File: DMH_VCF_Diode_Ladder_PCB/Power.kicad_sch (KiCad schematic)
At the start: 14 parts, among them J0 Conn_01x01, J100 IDC_02x08, J101 IDC_02x05

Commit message: Main schematic in progress
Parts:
- added C8, C9: 100nF, Capacitor_THT:C_Disc_D4.3mm_W1.9mm_P5.00mm, symbol Device:C
- added U1: TL074, Package_DIP:DIP-14_W7.62mm_Socket, symbol Amplifier_Operational:TL074
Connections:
- net +12V: now also C8.1, U1.4 (V+)
- net -12V: now also C9.2, U1.11 (V-)
- net GND: now also C8.2, C9.1

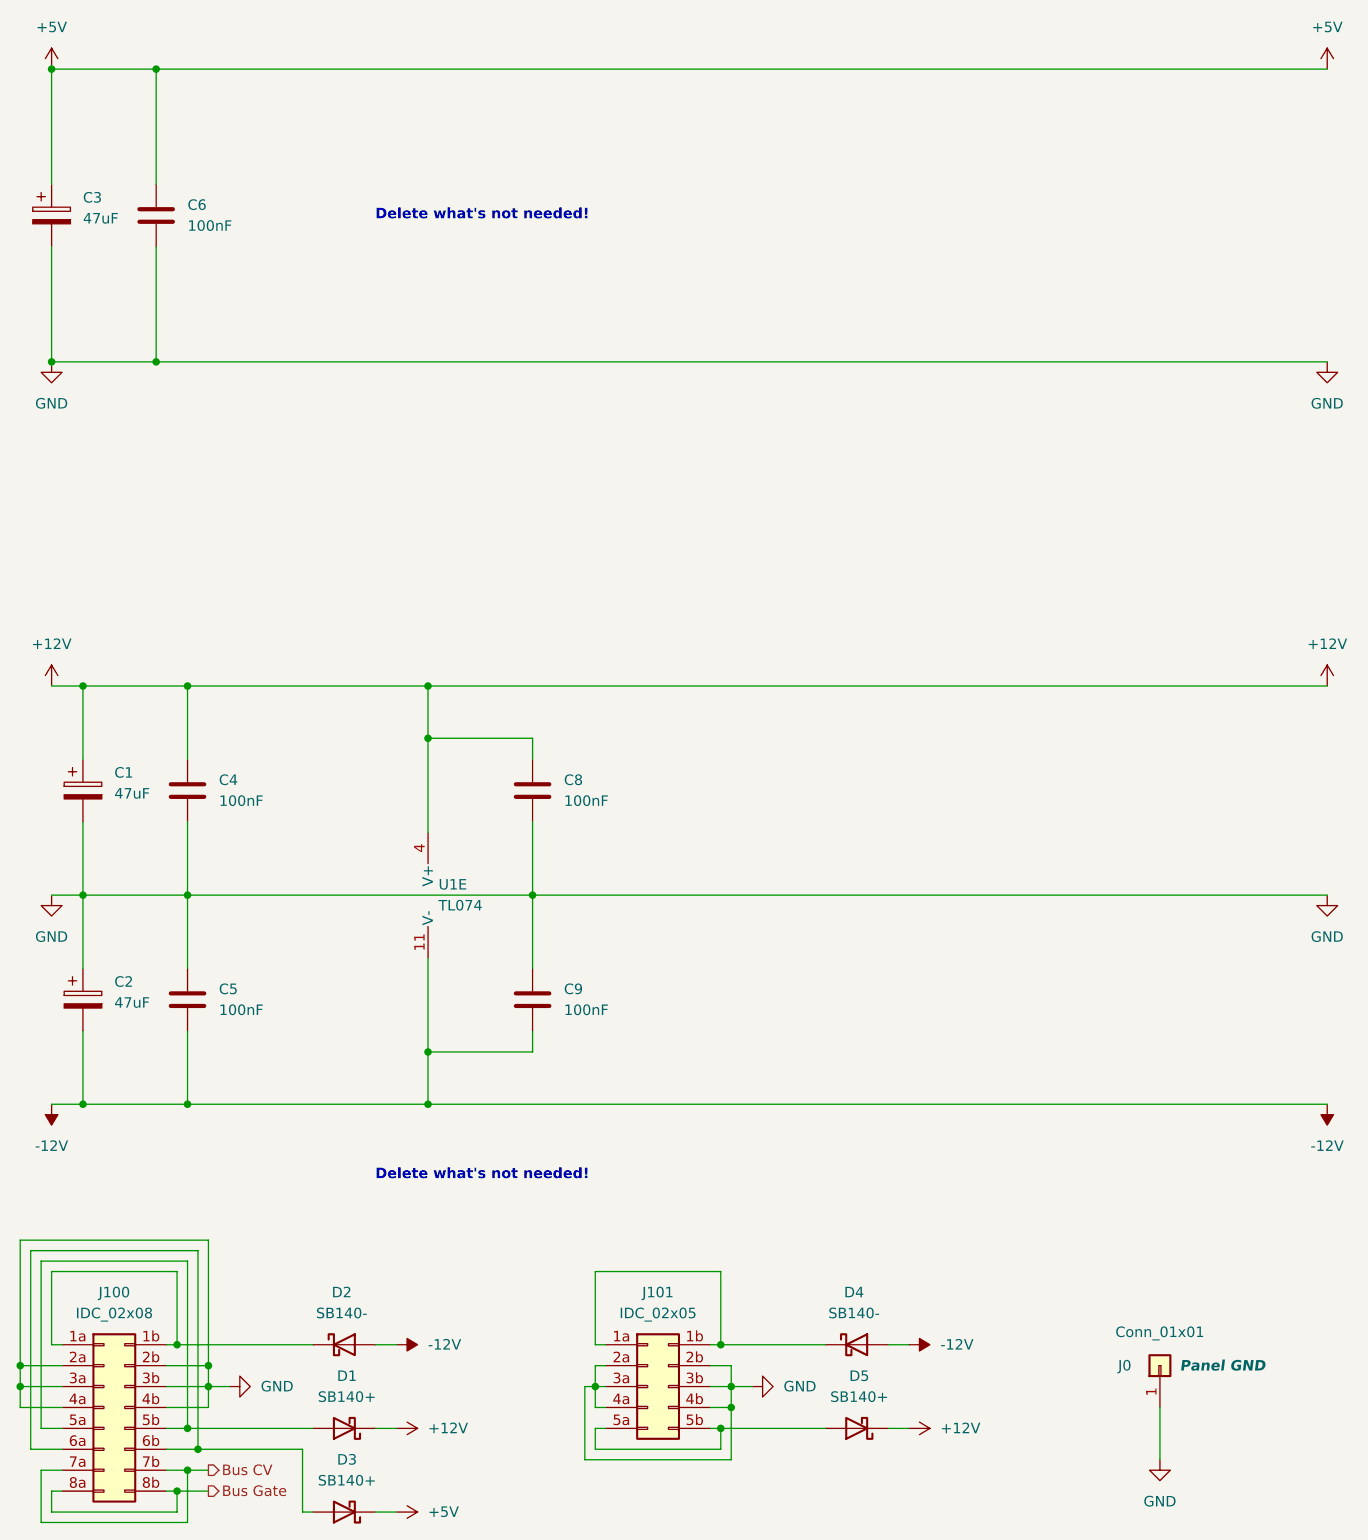
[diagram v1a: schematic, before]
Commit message: Finished schematic and added Bus CV 2 pot
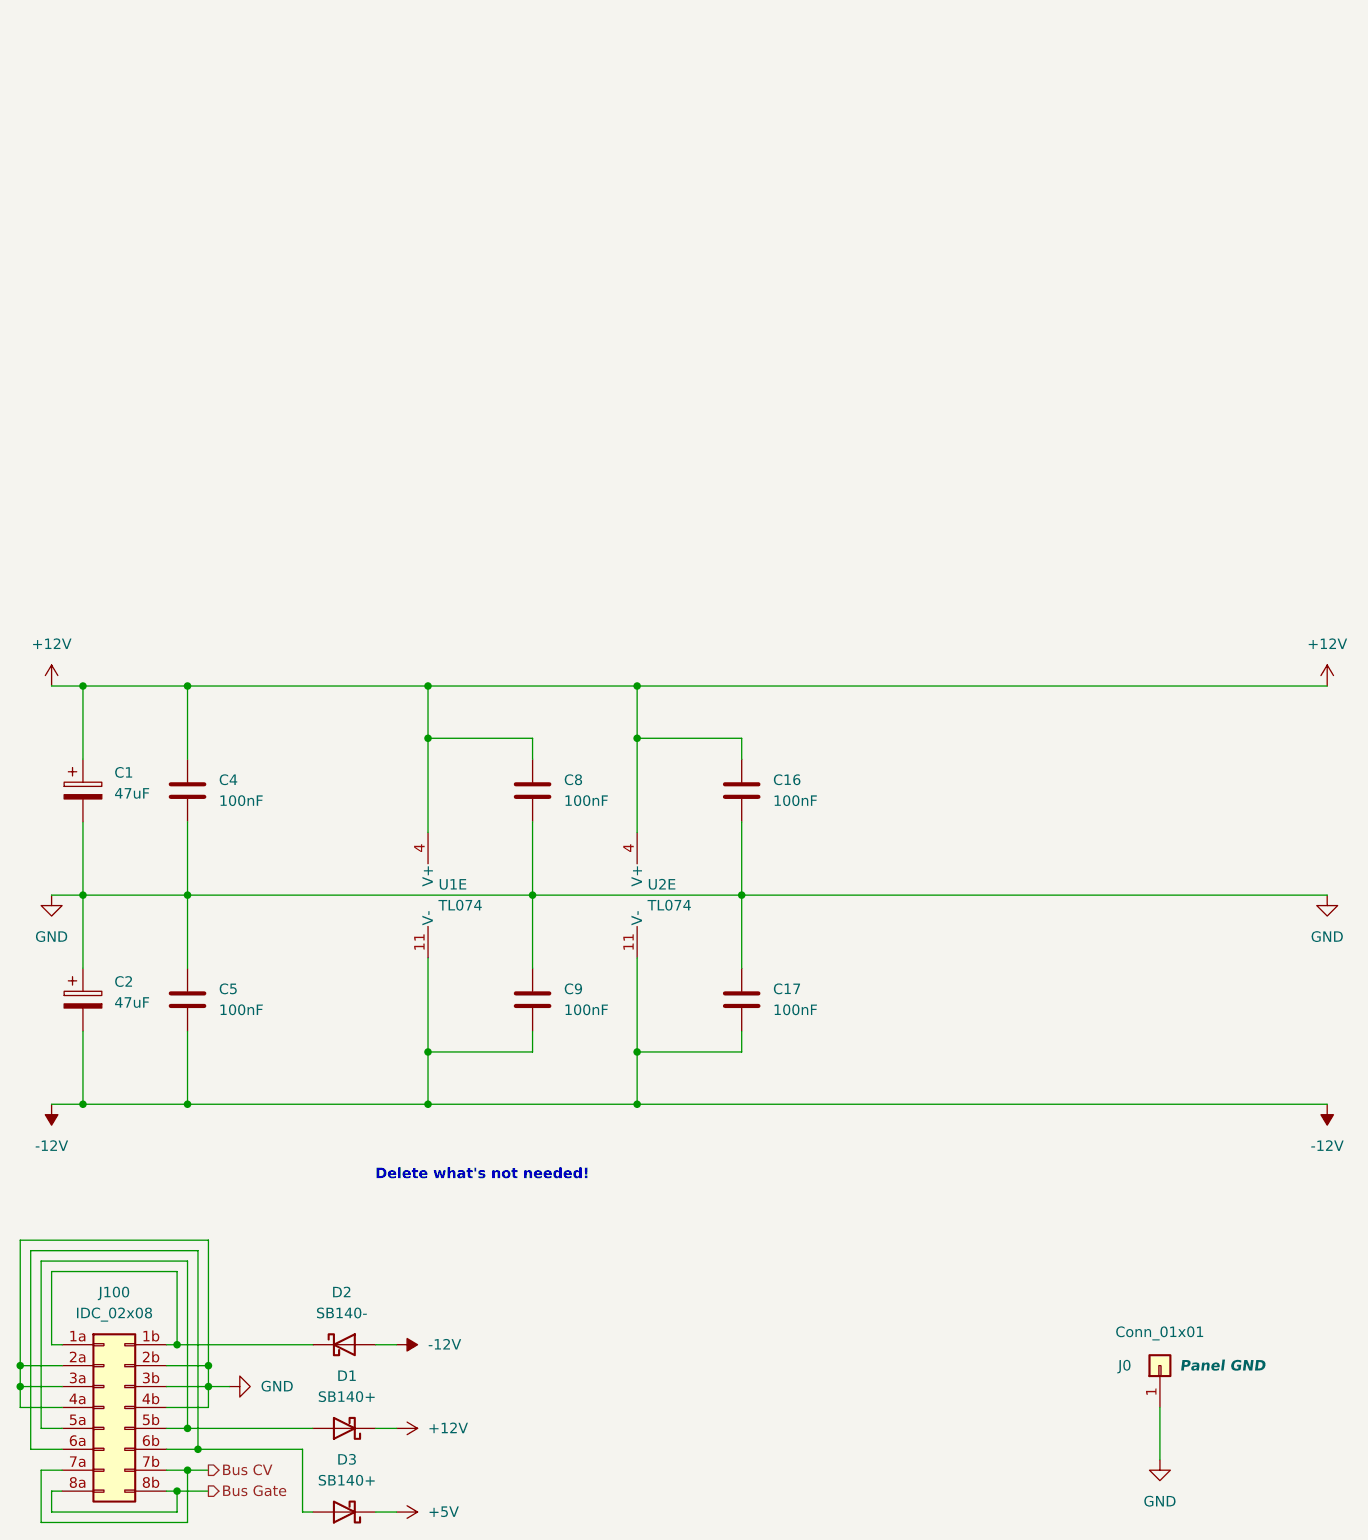
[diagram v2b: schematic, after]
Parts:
- removed C3: 47uF, Capacitor_THT:CP_Radial_D4.0mm_P1.50mm, symbol Device:C_Polarized
- removed C6: 100nF, Capacitor_THT:C_Disc_D4.3mm_W1.9mm_P5.00mm, symbol Device:C
- removed D4: SB140-, Diode_THT:D_DO-41_SOD81_P10.16mm_Horizontal, symbol SynthStuff:Power_Bus_Schotty_-
- removed D5: SB140+, Diode_THT:D_DO-41_SOD81_P10.16mm_Horizontal, symbol SynthStuff:Power_Bus_Schotty_+
- removed J101: IDC_02x05, SynthStuff:IDC-Header_2x05_P2.54mm_Vertical_Eurorack, symbol SynthStuff:Eurorack_Power_Connector_10Pin
- added C16, C17: 100nF, Capacitor_THT:C_Disc_D4.3mm_W1.9mm_P5.00mm, symbol Device:C
- added U2: TL074, Package_DIP:DIP-14_W7.62mm_Socket, symbol Amplifier_Operational:TL074
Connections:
- net +12V: now also C16.1, U2.4 (V+)
- net -12V: now also C17.2, U2.11 (V-)
- net GND: now also C16.2, C17.1

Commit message: Component placement in progress
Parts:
- removed D3: SB140+, Diode_THT:D_DO-41_SOD81_P10.16mm_Horizontal, symbol SynthStuff:Power_Bus_Schotty_+
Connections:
- net at J100.6a (Pin_6a): no longer J100.6b (Pin_6b)
- no-connect marks 0 -> 2
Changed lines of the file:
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@@
-	)
-	(junction
-		(at 35.56 187.96)
-		(diameter 0)
-		(color 0 0 0 0)
 	)
 	(junction
@@
 		(color 0 0 0 0)
 	)
+	(no_connect
+		(at 19.05 187.96)
+	)
+	(no_connect
+		(at 31.75 187.96)
+	)
 	(wire
 		(pts
@@
 	(wire
 		(pts
-			(xy 15.24 163.83) (xy 35.56 163.83)
-		)
-		(stroke
-			(width 0)
-			(type default)
-		)
-	)
-	(wire
-		(pts
 			(xy 63.5 139.7) (xy 63.5 146.05)
 		)
@@
 	(wire
 		(pts
-			(xy 35.56 163.83) (xy 35.56 187.96)
-		)
-		(stroke
-			(width 0)
-			(type default)
-		)
-	)
-	(wire
-		(pts
 			(xy 17.78 120.65) (xy 21.59 120.65)
 		)
@@
 	(wire
 		(pts
-			(xy 35.56 187.96) (xy 48.26 187.96)
-		)
-		(stroke
-			(width 0)
-			(type default)
-		)
-	)
-	(wire
-		(pts
 			(xy 21.59 120.65) (xy 34.29 120.65)
 		)
@@
 	(wire
 		(pts
-			(xy 31.75 187.96) (xy 35.56 187.96)
-		)
-		(stroke
-			(width 0)
-			(type default)
-		)
-	)
-	(wire
-		(pts
 			(xy 88.9 101.6) (xy 88.9 113.03)
 		)
@@
 	(wire
 		(pts
-			(xy 19.05 187.96) (xy 15.24 187.96)
-		)
-		(stroke
-			(width 0)
-			(type default)
-		)
-	)
-	(wire
-		(pts
-			(xy 48.26 195.58) (xy 49.53 195.58)
-		)
-		(stroke
-			(width 0)
-			(type default)
-		)
-	)
-	(wire
-		(pts
 			(xy 57.15 175.26) (xy 59.69 175.26)
 		)
@@
 	(wire
 		(pts
-			(xy 57.15 195.58) (xy 59.69 195.58)
-		)
-		(stroke
-			(width 0)
-			(type default)
-		)
-	)
-	(wire
-		(pts
 			(xy 21.59 137.16) (xy 21.59 146.05)
 		)
@@
 	(wire
 		(pts
-			(xy 48.26 187.96) (xy 48.26 195.58)
-		)
-		(stroke
-			(width 0)
-			(type default)
-		)
-	)
-	(wire
-		(pts
 			(xy 63.5 95.25) (xy 63.5 101.6)
 		)
@@
 		(pts
 			(xy 13.97 182.88) (xy 13.97 180.34)
-		)
-		(stroke
-			(width 0)
-			(type default)
-		)
-	)
-	(wire
-		(pts
-			(xy 15.24 187.96) (xy 15.24 163.83)
 		)
 		(stroke
@@
 	)
 	(symbol
-		(lib_id "power:+5V")
-		(at 59.69 195.58 270)
-		(unit 1)
-		(exclude_from_sim no)
-		(in_bom yes)
-		(on_board yes)
-		(dnp no)
-		(fields_autoplaced yes)
-		(property "Reference" "#PWR03"
-			(at 55.88 195.58 0)
-			(effects
-				(font
-					(size 1.27 1.27)
-				)
-				(hide yes)
-			)
-		)
-		(property "Value" "+5V"
-			(at 63.5 195.5799 90)
-			(effects
-				(font
-					(size 1.27 1.27)
-				)
-				(justify left)
-			)
-		)
-		(property "Footprint" ""
-			(at 59.69 195.58 0)
-			(effects
-				(font
-					(size 1.27 1.27)
-				)
-				(hide yes)
-			)
-		)
-		(property "Datasheet" ""
-			(at 59.69 195.58 0)
-			(effects
-				(font
-					(size 1.27 1.27)
-				)
-				(hide yes)
-			)
-		)
-		(property "Description" "Power symbol creates a global label with name \"+5V\""
-			(at 59.69 195.58 0)
-			(effects
-				(font
-					(size 1.27 1.27)
-				)
-				(hide yes)
-			)
-		)
-		(pin "1"
-		)
-		(instances
-			(project "DMH-Kosmo-10cm-PCB"
-				(path "/58f4306d-5387-4983-bb08-41a2313fd315/0cdf34b2-39cd-4d9e-981a-97cd34791509"
-					(reference "#PWR03")
-					(unit 1)
-				)
-			)
-		)
-	)
-	(symbol
 		(lib_id "power:GND")
 		(at 152.4 189.23 0)
@@
 					(unit 1)
 				)
-			)
-		)
-	)
-	(symbol
-		(lib_id "SynthStuff:Power_Bus_Schotty_+")
-		(at 53.34 195.58 180)
-		(unit 1)
-		(exclude_from_sim no)
-		(in_bom yes)
-		(on_board yes)
-		(dnp no)
-		(fields_autoplaced yes)
-		(property "Reference" "D3"
-			(at 53.6575 189.23 0)
-			(effects
-				(font
-					(size 1.27 1.27)
-				)
-			)
-		)
-		(property "Value" "SB140+"
-			(at 53.6575 191.77 0)
-			(effects
-				(font
-					(size 1.27 1.27)
-				)
-			)
-		)
-		(property "Footprint" "Diode_THT:D_DO-41_SOD81_P10.16mm_Horizontal"
-			(at 53.34 191.135 0)
-			(effects
-				(font
-					(size 1.27 1.27)
-				)
-				(hide yes)
-			)
-		)
-		(property "Datasheet" "http://www.diodes.com/_files/datasheets/ds23022.pdf"
-			(at 53.34 195.58 0)
-			(effects
-				(font
-					(size 1.27 1.27)
-				)
-				(hide yes)
-			)
-		)
-		(property "Description" "40V 1A Schottky Barrier Rectifier Diode, DO-41"
-			(at 53.34 195.58 0)
-			(effects
-				(font
-					(size 1.27 1.27)
-				)
-				(hide yes)
-			)
-		)
-		(pin "2"
-		)
-		(pin "1"
-		)
-		(instances
-			(project "DMH-Kosmo-10cm-PCB"
-				(path "/58f4306d-5387-4983-bb08-41a2313fd315/0cdf34b2-39cd-4d9e-981a-97cd34791509"
-					(reference "D3")
-					(unit 1)
-				)
